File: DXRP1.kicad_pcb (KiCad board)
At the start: 2 copper layers, 50 x 50 mm, 55 parts, among them J1 USB_B_Micro, J11 5v, J12 VIN, J13 MB, J14 MA, J15 Servo 5V, J16 Servo signal, J17 Servo GND, J18 GND pad, J2 I2C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

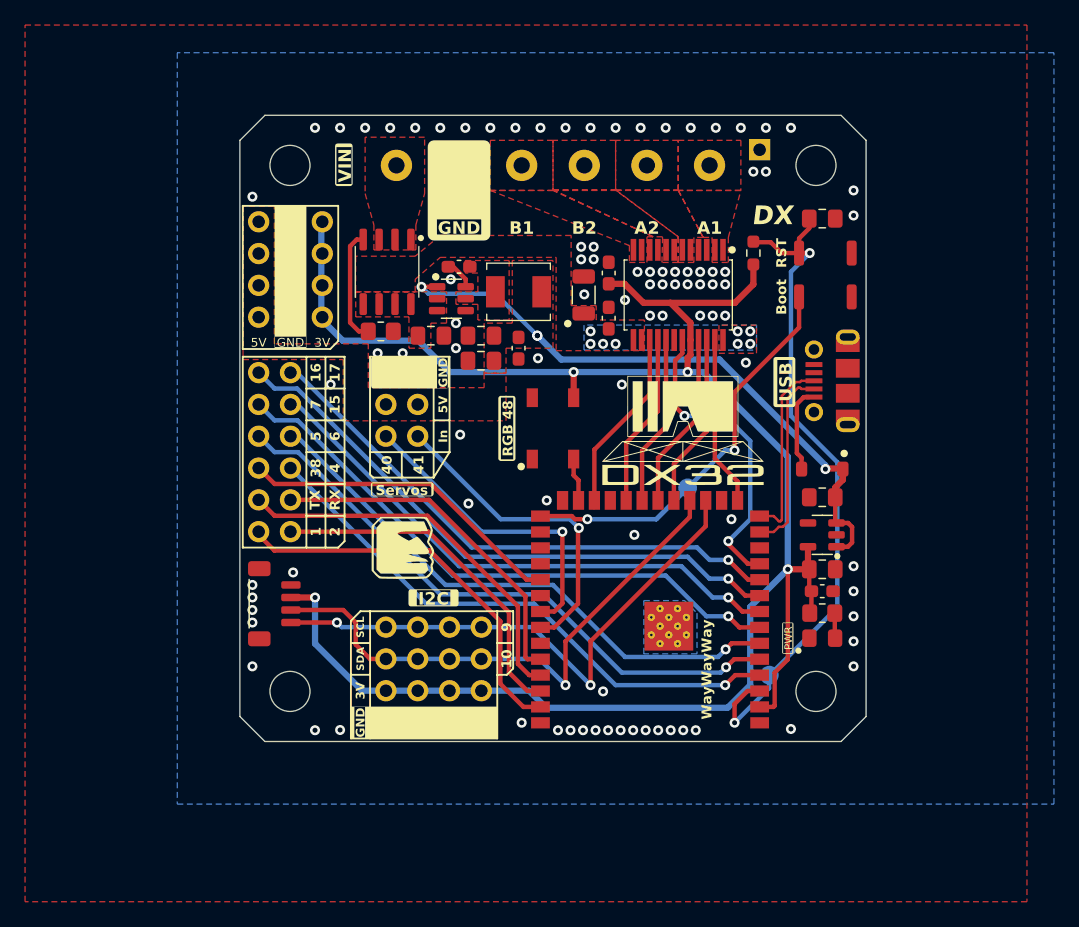
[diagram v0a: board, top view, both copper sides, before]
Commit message: Revision 1.1
Added proper USB backpowering protection circuit
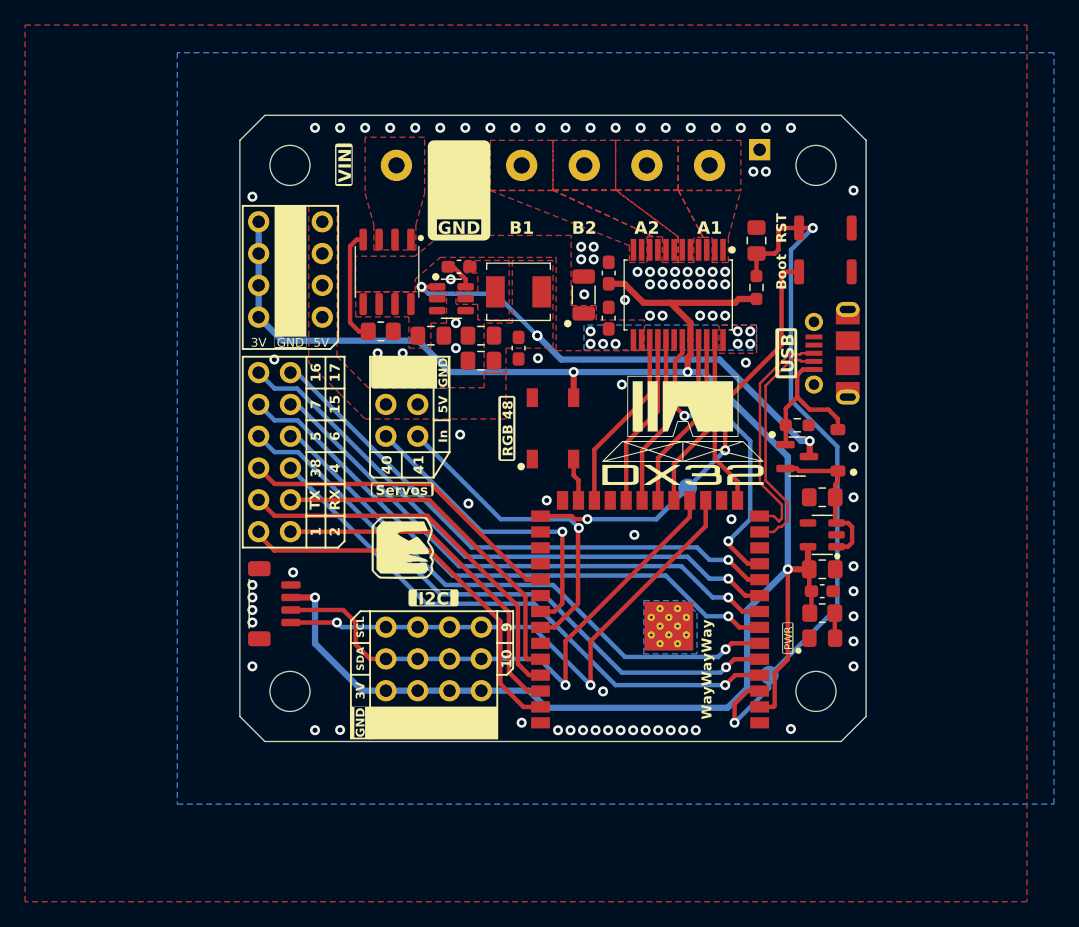
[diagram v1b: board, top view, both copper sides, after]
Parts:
- added Q1: AO3401A, Package_TO_SOT_SMD:SOT-23, F.Cu at (144.5, 87.2)
- added R2: 100k, Resistor_SMD:R_0603_1608Metric_Pad0.98x0.95mm_HandSolder, F.Cu at (144.5, 84.8)
- moved C1 5.53 mm to (141.2, 70.0), turned to 90 degrees
- moved J11 5.08 mm to (106.6, 68.5)
- moved J7 5.08 mm to (101.5, 68.5)
- moved R1 2.76 mm to (141.2, 73.8)
- moved J1 2.20 mm to (147.3, 79.0)
- moved SW1 2.00 mm to (146.8, 72.5)
- moved SW2 2.00 mm to (146.8, 69.0)
- moved D1 1.95 mm to (147.8, 86.8), turned to 90 degrees
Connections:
- net VBUS renamed VMotor
- C4 pad 1: +5V -> Net-(D1-K)
- D1 pad 1: +5V -> Net-(D1-K)
- U3 pad 1: +5V -> Net-(D1-K)
- U3 pad 3: +5V -> Net-(D1-K)
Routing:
- net Net-(D1-K): track 0.00 -> 12.6 mm
- net +5V: track 49.7 -> 38.6 mm
- net VUSB: track 6.61 -> 12.3 mm
- net /USB_D+: track 14.9 -> 18.9 mm
- net /USB_D-: track 14.9 -> 18.9 mm
- net +3.3V: track 154.5 -> 157.7 mm
- net /BOOT: track 35.9 -> 38.1 mm
- net /RESET: track 54.9 -> 57.1 mm
- net GND: vias 93 -> 94
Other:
- board text added: "V1.1"
- board text removed: "DX"
